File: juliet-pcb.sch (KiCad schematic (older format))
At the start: 94 parts, among them SW0 KEYSW, SW1 KEYSW, SW10 KEYSW, SW11 KEYSW, SW12 KEYSW, SW13 KEYSW, SW14 KEYSW, SW15 KEYSW, SW16 KEYSW, SW17 KEYSW, SW18 KEYSW, SW19 KEYSW, SW2 KEYSW, SW20 KEYSW, SW21 KEYSW, SW22 KEYSW, SW23 KEYSW, SW24 KEYSW, SW25 KEYSW, SW26 KEYSW, SW27 KEYSW, SW28 KEYSW, SW29 KEYSW, SW3 KEYSW, SW30 KEYSW, SW31 KEYSW, SW32 KEYSW, SW33 KEYSW, SW34 KEYSW, SW35 KEYSW, SW36 KEYSW, SW37 KEYSW, SW38 KEYSW, SW39 KEYSW, SW4 KEYSW, SW40 KEYSW, SW41 KEYSW, SW42 KEYSW, SW43 KEYSW, SW44 KEYSW, SW45 KEYSW, SW46 KEYSW, SW47 KEYSW, SW5 KEYSW, SW6 KEYSW, SW7 KEYSW, SW8 KEYSW, SW9 KEYSW, U1 Pro_Micro

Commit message: lol fixed
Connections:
- net GND: now also U1.23 (GND), U1.3 (GND), U1.4 (GND)
- net row0: now also U1.20 (A3(PF4)); no longer U1.3 (GND)
- net row3: now also U1.19 (A2(PF5)); no longer U1.4 (GND)
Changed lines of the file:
@@
 Text GLabel 7200 4500 2    50   Input ~ 0
 reset
-Text GLabel 5900 4500 0    50   Input ~ 0
+Text GLabel 7200 4700 2    50   Input ~ 0
 row0
 Text GLabel 5900 4400 0    50   Input ~ 0
@@
 Text GLabel 5900 4300 0    50   Input ~ 0
 row2
-Text GLabel 5900 4600 0    50   Input ~ 0
+Text GLabel 7200 4800 2    50   Input ~ 0
 row3
 Text GLabel 5900 4700 0    50   Input ~ 0
@@
 Text GLabel 7200 4300 2    50   Input ~ 0
 RAW
+Text GLabel 5900 4500 0    50   Input ~ 0
+GND
+Text GLabel 5900 4600 0    50   Input ~ 0
+GND
+Text GLabel 7200 4400 2    50   Input ~ 0
+GND
 $EndSCHEMATC

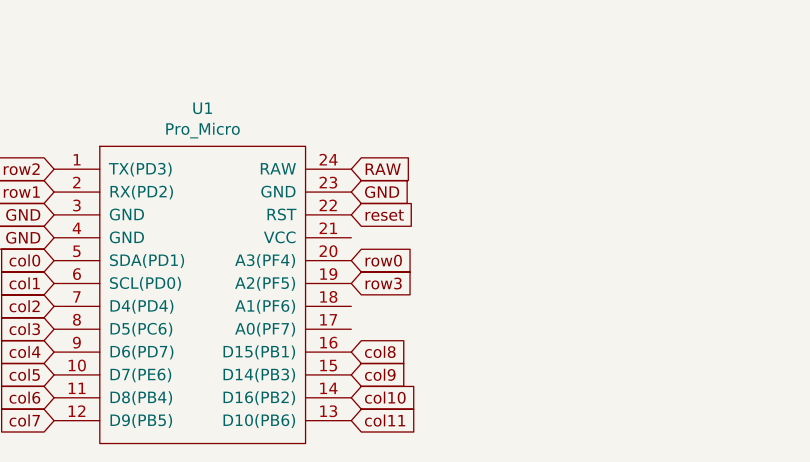
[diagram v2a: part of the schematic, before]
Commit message: Updated pro micro location
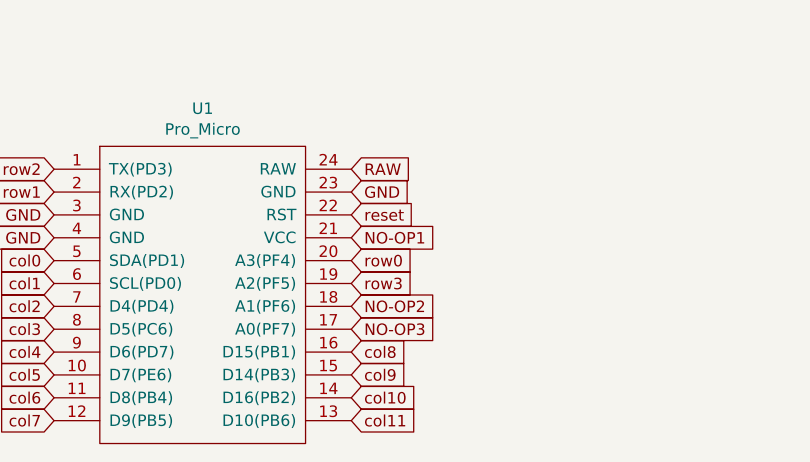
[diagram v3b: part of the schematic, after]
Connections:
- net NO-OP3: now reaches U1.17 (A0(PF7))
- net NO-OP2: now reaches U1.18 (A1(PF6))
- net NO-OP1: now reaches U1.21 (VCC)
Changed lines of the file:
@@
 Text GLabel 7200 4700 2    50   Input ~ 0
 row0
+Text GLabel 7200 4600 2    50   Input ~ 0
+NO-OP1
+Text GLabel 7200 4900 2    50   Input ~ 0
+NO-OP2
+Text GLabel 7200 5000 2    50   Input ~ 0
+NO-OP3
 $EndSCHEMATC

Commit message: Fixed a lot of issues.
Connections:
- net row0: now also U1.19 (A2(PF5)); no longer U1.20 (A3(PF4))
- net row3: now also U1.20 (A3(PF4)); no longer U1.19 (A2(PF5))
- net NO-OP1: no longer names the net of U1.21 (VCC)
- net NO-OP2: no longer names the net of U1.18 (A1(PF6))
- net NO-OP3: no longer names the net of U1.17 (A0(PF7))
- no-connect marks 0 -> 3
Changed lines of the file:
@@
 Text GLabel 7200 4400 2    50   Input ~ 0
 GND
+Text GLabel 7200 4700 2    50   Input ~ 0
+row3
 Text GLabel 7200 4800 2    50   Input ~ 0
-row3
-Text GLabel 7200 4700 2    50   Input ~ 0
 row0
-Text GLabel 7200 4600 2    50   Input ~ 0
-NO-OP1
-Text GLabel 7200 4900 2    50   Input ~ 0
-NO-OP2
-Text GLabel 7200 5000 2    50   Input ~ 0
-NO-OP3
+NoConn ~ 7200 4600
+NoConn ~ 7200 4900
+NoConn ~ 7200 5000
 $EndSCHEMATC
